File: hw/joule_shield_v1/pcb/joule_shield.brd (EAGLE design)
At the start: 60 x 40 mm, 144 parts, among them J1 MF-CON-MICROUSB-RIGHT, J4 USB_AUSB_A_SMT_RA, J5 JST-ZH5SMT_RA, J6 INTEL_JOULE_J6, J7 INTEL_JOULE_J7, J8 DM3ATDM3AT, Q1 NFETEMT3F, Q2 NFETEMT3F, Q3 NFETEMT3F, Q4 NFETEMT3F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

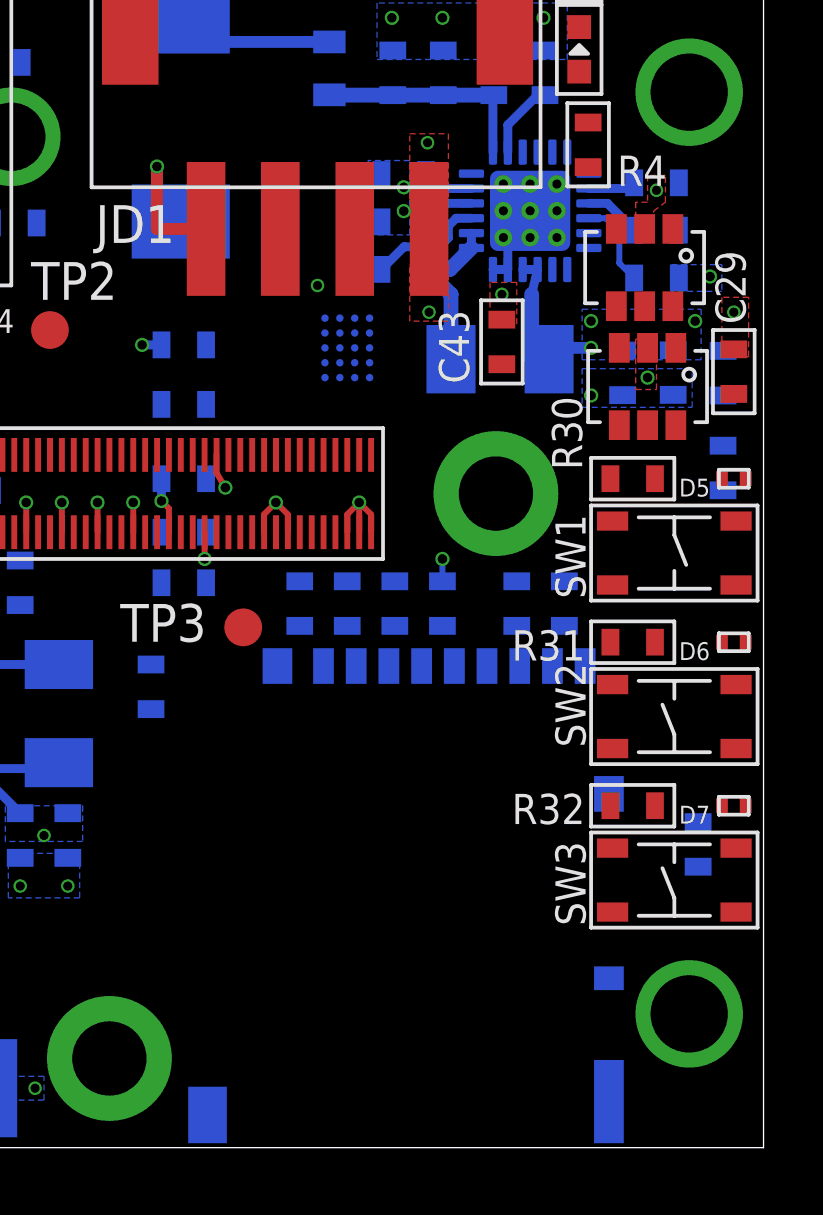
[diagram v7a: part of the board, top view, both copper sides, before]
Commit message: joule shield: board title silks
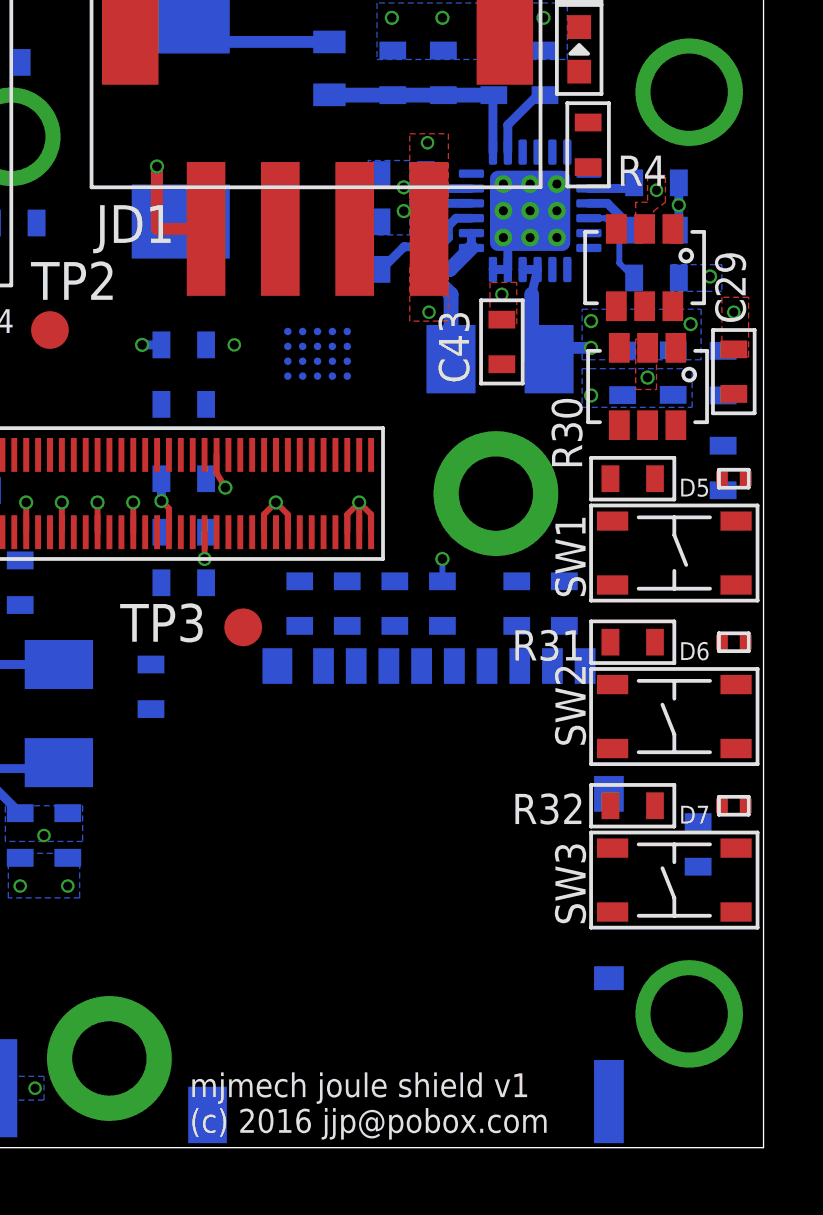
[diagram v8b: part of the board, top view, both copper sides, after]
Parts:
- moved U9 1.02 mm to (45.0, 26.7), turned to 180 degrees
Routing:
- net VSYS: track 31.9 -> 33.5 mm, vias 17 -> 18
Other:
- board text added: "(c) 2016 jjp@pobox.com"
- board text added: "mjmech joule shield v1"
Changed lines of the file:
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@@
 <wire x1="60" y1="40" x2="0" y2="40" width="0" layer="20"/>
 <wire x1="0" y1="40" x2="0" y2="0" width="0" layer="20"/>
+<text x="40.7" y="1.7" size="0.8" layer="21" font="vector">mjmech joule shield v1</text>
+<text x="40.7" y="0.5" size="0.8" layer="21" font="vector">(c) 2016 jjp@pobox.com</text>
 </plain>
 <attributes>
@@
 <attribute name="NAME" x="20.5" y="10.6" size="1.016" layer="26" font="vector" ratio="16" rot="MR180"/>
 </element>
-<element name="U9" library="joule_shield" package="S-PBGA-N20" value="SN74AVCA406L" x="46" y="26.9" smashed="yes" rot="MR270">
-<attribute name="NAME" x="44.4" y="28.4" size="0.8" layer="22" font="vector" rot="MR270"/>
+<element name="U9" library="joule_shield" package="S-PBGA-N20" value="SN74AVCA406L" x="45" y="26.7" smashed="yes" rot="MR180">
+<attribute name="NAME" x="43.5" y="25.1" size="0.8" layer="22" font="vector" rot="MR180"/>
 </element>
 <element name="R41" library="mf_passives" package="R0603" value="100k" x="47.6" y="18.3" smashed="yes" rot="MR270">
@@
 </polygon>
 <via x="26.1" y="2.7" extent="1-16" drill="0.3048"/>
-<via x="45" y="29" extent="1-16" drill="0.3048"/>
+<via x="42.2" y="27" extent="1-16" drill="0.3048"/>
 <wire x1="7.2" y1="38.4" x2="8" y2="38.4" width="0.3" layer="16"/>
 <wire x1="8" y1="38.4" x2="9.295" y2="38.4" width="0.3" layer="16"/>
@@
 <wire x1="39.75" y1="19" x2="41.202" y2="19.802" width="0" layer="19" extent="1-16"/>
 <wire x1="24.5" y1="30.42" x2="26" y2="28.95" width="0" layer="19" extent="1-16"/>
-<wire x1="45.75" y1="26.9" x2="45" y2="29" width="0" layer="19" extent="16-16"/>
-<wire x1="46.25" y1="26.9" x2="45.75" y2="26.9" width="0" layer="19" extent="16-16"/>
 <wire x1="4" y1="11.5" x2="4" y2="13.8" width="0" layer="19" extent="1-1"/>
 <wire x1="17.75" y1="34" x2="17.5" y2="36.35" width="0" layer="19" extent="1-16"/>
@@
 <wire x1="4" y1="21.2" x2="4.25" y2="18.9" width="0" layer="19" extent="1-1"/>
 <wire x1="2.75" y1="9.2" x2="4" y2="11.5" width="0" layer="19" extent="1-1"/>
+<wire x1="45" y1="26.95" x2="42.2" y2="27" width="0" layer="19" extent="16-16"/>
+<wire x1="45" y1="26.45" x2="45" y2="26.95" width="0" layer="19" extent="16-16"/>
 <wire x1="11.45" y1="27.2" x2="14.3" y2="27.6" width="0" layer="19" extent="16-16"/>
 <wire x1="50.7" y1="16.2" x2="49.2" y2="19.05" width="0" layer="19" extent="16-16"/>
@@
 <via x="54.2" y="26.9" extent="1-16" drill="0.32"/>
 <via x="54.2" y="27.8" extent="1-16" drill="0.32"/>
-<via x="57.7" y="27.8" extent="1-16" drill="0.32"/>
+<via x="57.55" y="27.7" extent="1-16" drill="0.32"/>
 <polygon width="0.1" layer="16">
 <vertex x="1.9" y="15.8"/>
@@
 <wire x1="12.102" y1="4.3" x2="12.102" y2="3.602" width="0.2" layer="1"/>
 <wire x1="12.102" y1="3.602" x2="11.9" y2="3.4" width="0.2" layer="1"/>
-<wire x1="57.15" y1="32.45" x2="57.15" y2="30.86" width="0" layer="19" extent="16-16"/>
-<wire x1="57.7" y1="27.8" x2="57.15" y2="30.86" width="0" layer="19" extent="16-16"/>
+<via x="57.15" y="31.7" extent="1-16" drill="0.32"/>
 <wire x1="4.25" y1="22.5" x2="4.9" y2="22.75" width="0" layer="19" extent="1-16"/>
 <wire x1="4.25" y1="12.8" x2="4.25" y2="16" width="0" layer="19" extent="1-16"/>
 <wire x1="4.25" y1="30.8" x2="4.9" y2="23.6" width="0" layer="19" extent="1-1"/>
+<wire x1="57.15" y1="30.86" x2="57.15" y2="31.7" width="0.3" layer="16"/>
+<wire x1="57.15" y1="31.7" x2="57.15" y2="32.45" width="0.3" layer="16"/>
 </signal>
 <signal name="V3P3V">
@@
 <contactref element="U9" pad="A5"/>
 <contactref element="R26" pad="P$1"/>
-<wire x1="41.25" y1="20.7" x2="45.25" y2="25.9" width="0" layer="19" extent="16-16"/>
+<wire x1="41.25" y1="20.7" x2="46" y2="25.95" width="0" layer="19" extent="16-16"/>
 <wire x1="41.25" y1="19" x2="41.25" y2="20.7" width="0" layer="19" extent="16-16"/>
 <wire x1="57.8" y1="10.95" x2="41.25" y2="19" width="0" layer="19" extent="16-16"/>
@@
 <contactref element="U9" pad="D1"/>
 <contactref element="R44" pad="P$2"/>
-<wire x1="53.3" y1="17.55" x2="46.75" y2="27.9" width="0" layer="19" extent="16-16"/>
+<wire x1="53.3" y1="17.55" x2="44" y2="27.45" width="0" layer="19" extent="16-16"/>
 <wire x1="52.9" y1="16.2" x2="53.3" y2="17.55" width="0" layer="19" extent="16-16"/>
 </signal>
@@
 <contactref element="U9" pad="C4"/>
 <contactref element="R43" pad="P$2"/>
-<wire x1="44.4" y1="17.55" x2="46.25" y2="26.4" width="0" layer="19" extent="16-16"/>
+<wire x1="44.4" y1="17.55" x2="45.5" y2="26.95" width="0" layer="19" extent="16-16"/>
 <wire x1="45.2" y1="16.2" x2="44.4" y2="17.55" width="0" layer="19" extent="16-16"/>
 </signal>
@@
 <contactref element="U9" pad="D4"/>
 <contactref element="R42" pad="P$2"/>
-<wire x1="46" y1="17.55" x2="46.75" y2="26.4" width="0" layer="19" extent="16-16"/>
+<wire x1="46" y1="17.55" x2="45.5" y2="27.45" width="0" layer="19" extent="16-16"/>
 <wire x1="46.3" y1="16.2" x2="46" y2="17.55" width="0" layer="19" extent="16-16"/>
 </signal>
@@
 <contactref element="U9" pad="C2"/>
 <contactref element="R41" pad="P$2"/>
-<wire x1="47.6" y1="17.55" x2="46.25" y2="27.4" width="0" layer="19" extent="16-16"/>
+<wire x1="47.6" y1="17.55" x2="44.5" y2="26.95" width="0" layer="19" extent="16-16"/>
 <wire x1="47.4" y1="16.2" x2="47.6" y2="17.55" width="0" layer="19" extent="16-16"/>
 </signal>
@@
 <contactref element="J8" pad="5"/>
 <contactref element="U9" pad="D3"/>
-<wire x1="49.6" y1="16.2" x2="46.75" y2="26.9" width="0" layer="19" extent="16-16"/>
+<wire x1="49.6" y1="16.2" x2="45" y2="27.45" width="0" layer="19" extent="16-16"/>
 </signal>
 <signal name="SDCARD_CD">
@@
 <contactref element="J6" pad="81"/>
 <contactref element="U9" pad="B2"/>
-<wire x1="43.202" y1="23.3" x2="45.75" y2="27.4" width="0" layer="19" extent="1-16"/>
+<wire x1="43.202" y1="23.3" x2="44.5" y2="26.45" width="0" layer="19" extent="1-16"/>
 </signal>
 <signal name="SDCARD_D1">
 <contactref element="J6" pad="83"/>
 <contactref element="U9" pad="A2"/>
-<wire x1="43.602" y1="23.3" x2="45.25" y2="27.4" width="0" layer="19" extent="1-16"/>
+<wire x1="43.602" y1="23.3" x2="44.5" y2="25.95" width="0" layer="19" extent="1-16"/>
 </signal>
 <signal name="SDCARD_D2">
 <contactref element="J6" pad="85"/>
 <contactref element="U9" pad="B4"/>
-<wire x1="44.002" y1="23.3" x2="45.75" y2="26.4" width="0" layer="19" extent="1-16"/>
+<wire x1="44.002" y1="23.3" x2="45.5" y2="26.45" width="0" layer="19" extent="1-16"/>
 </signal>
 <signal name="SDCARD_D3">
 <contactref element="J6" pad="87"/>
 <contactref element="U9" pad="A4"/>
-<wire x1="44.402" y1="23.3" x2="45.25" y2="26.4" width="0" layer="19" extent="1-16"/>
+<wire x1="44.402" y1="23.3" x2="45.5" y2="25.95" width="0" layer="19" extent="1-16"/>
 </signal>
 <signal name="SDCARD_CMD">
 <contactref element="J6" pad="89"/>
 <contactref element="U9" pad="B1"/>
-<wire x1="44.802" y1="23.3" x2="45.75" y2="27.9" width="0" layer="19" extent="1-16"/>
+<wire x1="44.802" y1="23.3" x2="44" y2="26.45" width="0" layer="19" extent="1-16"/>
 </signal>
 <signal name="SDCARD_CLK">
 <contactref element="J6" pad="75"/>
 <contactref element="U9" pad="A3"/>
-<wire x1="42.002" y1="23.3" x2="45.25" y2="26.9" width="0" layer="19" extent="1-16"/>
+<wire x1="42.002" y1="23.3" x2="45" y2="25.95" width="0" layer="19" extent="1-16"/>
 </signal>
 <signal name="SDCARD_CLK_FB">
 <contactref element="J6" pad="77"/>
 <contactref element="U9" pad="A1"/>
-<wire x1="42.402" y1="23.3" x2="45.25" y2="27.9" width="0" layer="19" extent="1-16"/>
+<wire x1="42.402" y1="23.3" x2="44" y2="25.95" width="0" layer="19" extent="1-16"/>
 </signal>
 <signal name="SDCARD_VCCB">
@@
 <contactref element="R44" pad="P$1"/>
 <contactref element="R45" pad="P$1"/>
-<wire x1="41.25" y1="25" x2="46.75" y2="25.9" width="0" layer="19" extent="16-16"/>
-<wire x1="41.25" y1="27" x2="41.25" y2="25" width="0" layer="19" extent="16-16"/>
+<wire x1="41.25" y1="27" x2="46" y2="27.45" width="0" layer="19" extent="16-16"/>
+<wire x1="41.25" y1="25" x2="41.25" y2="27" width="0" layer="19" extent="16-16"/>
 <wire x1="41.25" y1="22.5" x2="41.25" y2="25" width="0" layer="19" extent="16-16"/>
 <wire x1="44.4" y1="19.05" x2="41.25" y2="22.5" width="0" layer="19" extent="16-16"/>
@@
 <contactref element="J6" pad="90"/>
 <contactref element="U9" pad="B5"/>
-<wire x1="44.802" y1="20.7" x2="45.75" y2="25.9" width="0" layer="19" extent="1-16"/>
+<wire x1="44.802" y1="20.7" x2="46" y2="26.45" width="0" layer="19" extent="1-16"/>
 </signal>
 <signal name="SDCARD_LVL_DAT_DIR">
@@
 <contactref element="U9" pad="C1"/>
 <contactref element="U9" pad="C5"/>
-<wire x1="46.25" y1="25.9" x2="46.25" y2="27.9" width="0" layer="19" extent="16-16"/>
-<wire x1="40.402" y1="23.3" x2="46.25" y2="25.9" width="0" layer="19" extent="1-16"/>
+<wire x1="44" y1="26.95" x2="46" y2="26.95" width="0" layer="19" extent="16-16"/>
+<wire x1="40.402" y1="23.3" x2="44" y2="26.95" width="0" layer="19" extent="1-16"/>
 </signal>
 <signal name="N$69">
@@
 <contactref element="U9" pad="D2"/>
 <contactref element="R45" pad="P$2"/>
-<wire x1="51.7" y1="17.55" x2="46.75" y2="27.4" width="0" layer="19" extent="16-16"/>
+<wire x1="51.7" y1="17.55" x2="44.5" y2="27.45" width="0" layer="19" extent="16-16"/>
 <wire x1="51.8" y1="16.2" x2="51.7" y2="17.55" width="0" layer="19" extent="16-16"/>
 </signal>
